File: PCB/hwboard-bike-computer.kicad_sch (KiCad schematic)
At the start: 0 parts

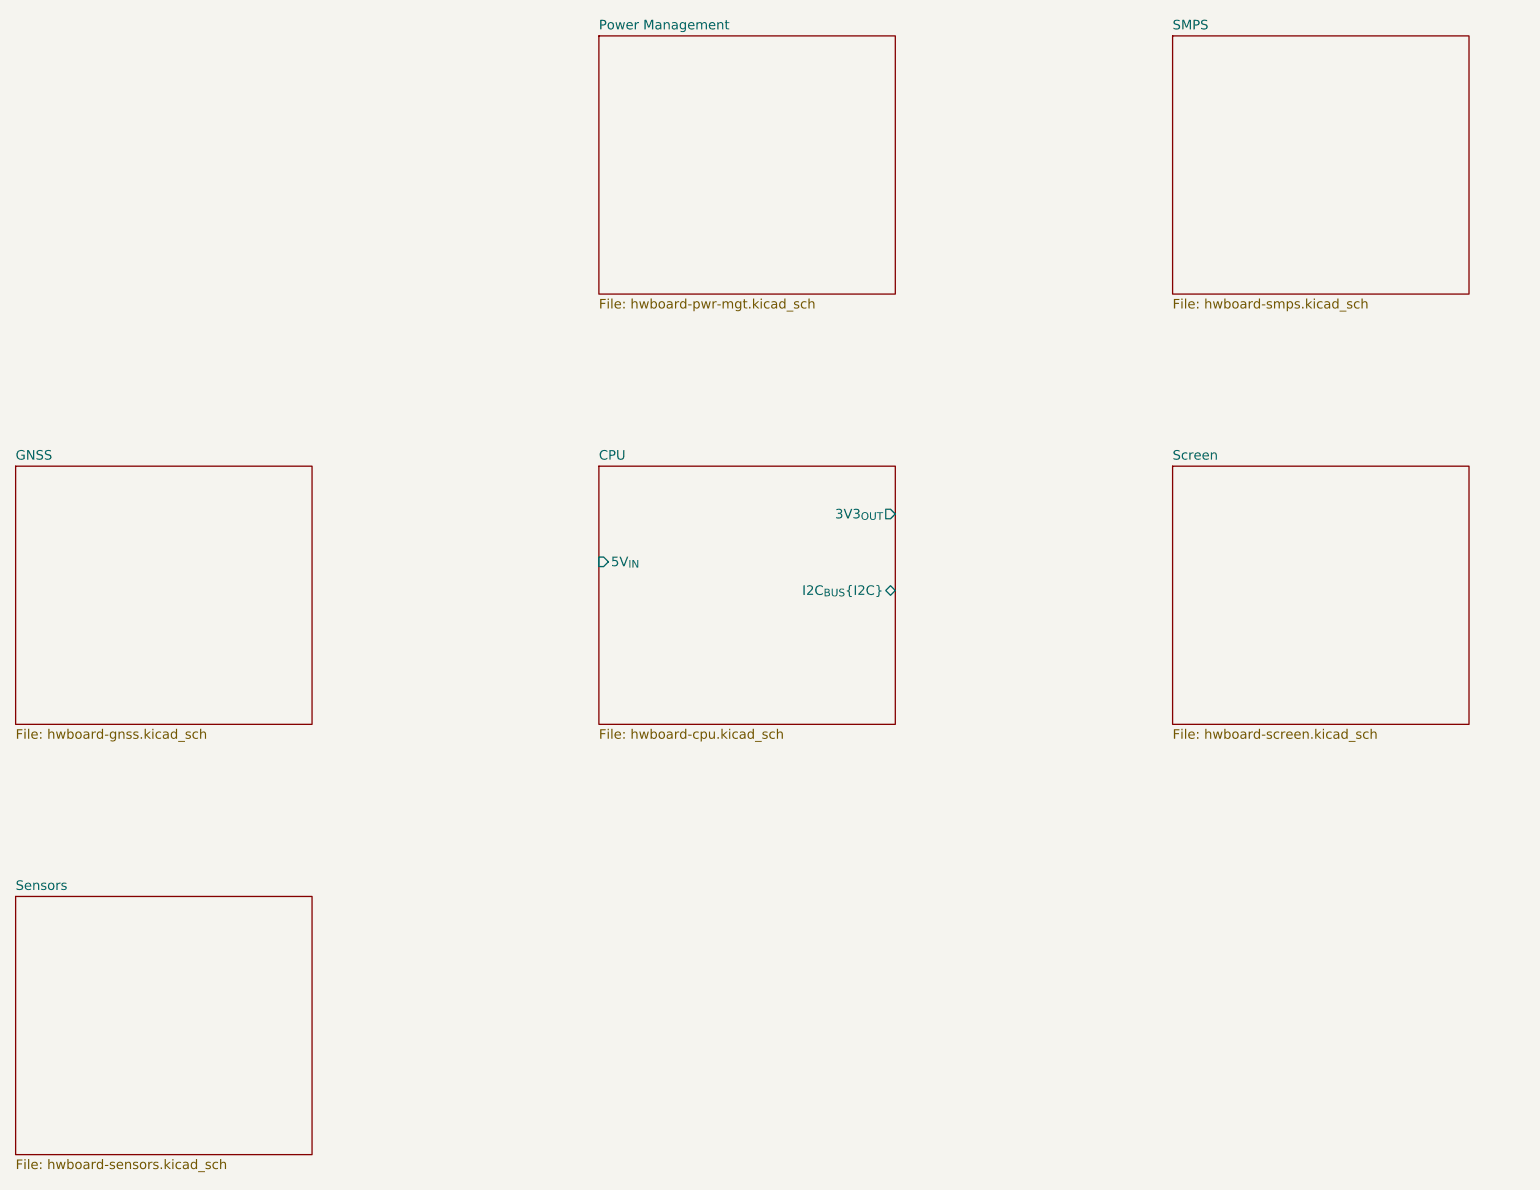
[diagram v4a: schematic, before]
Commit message: add dc dc schematic
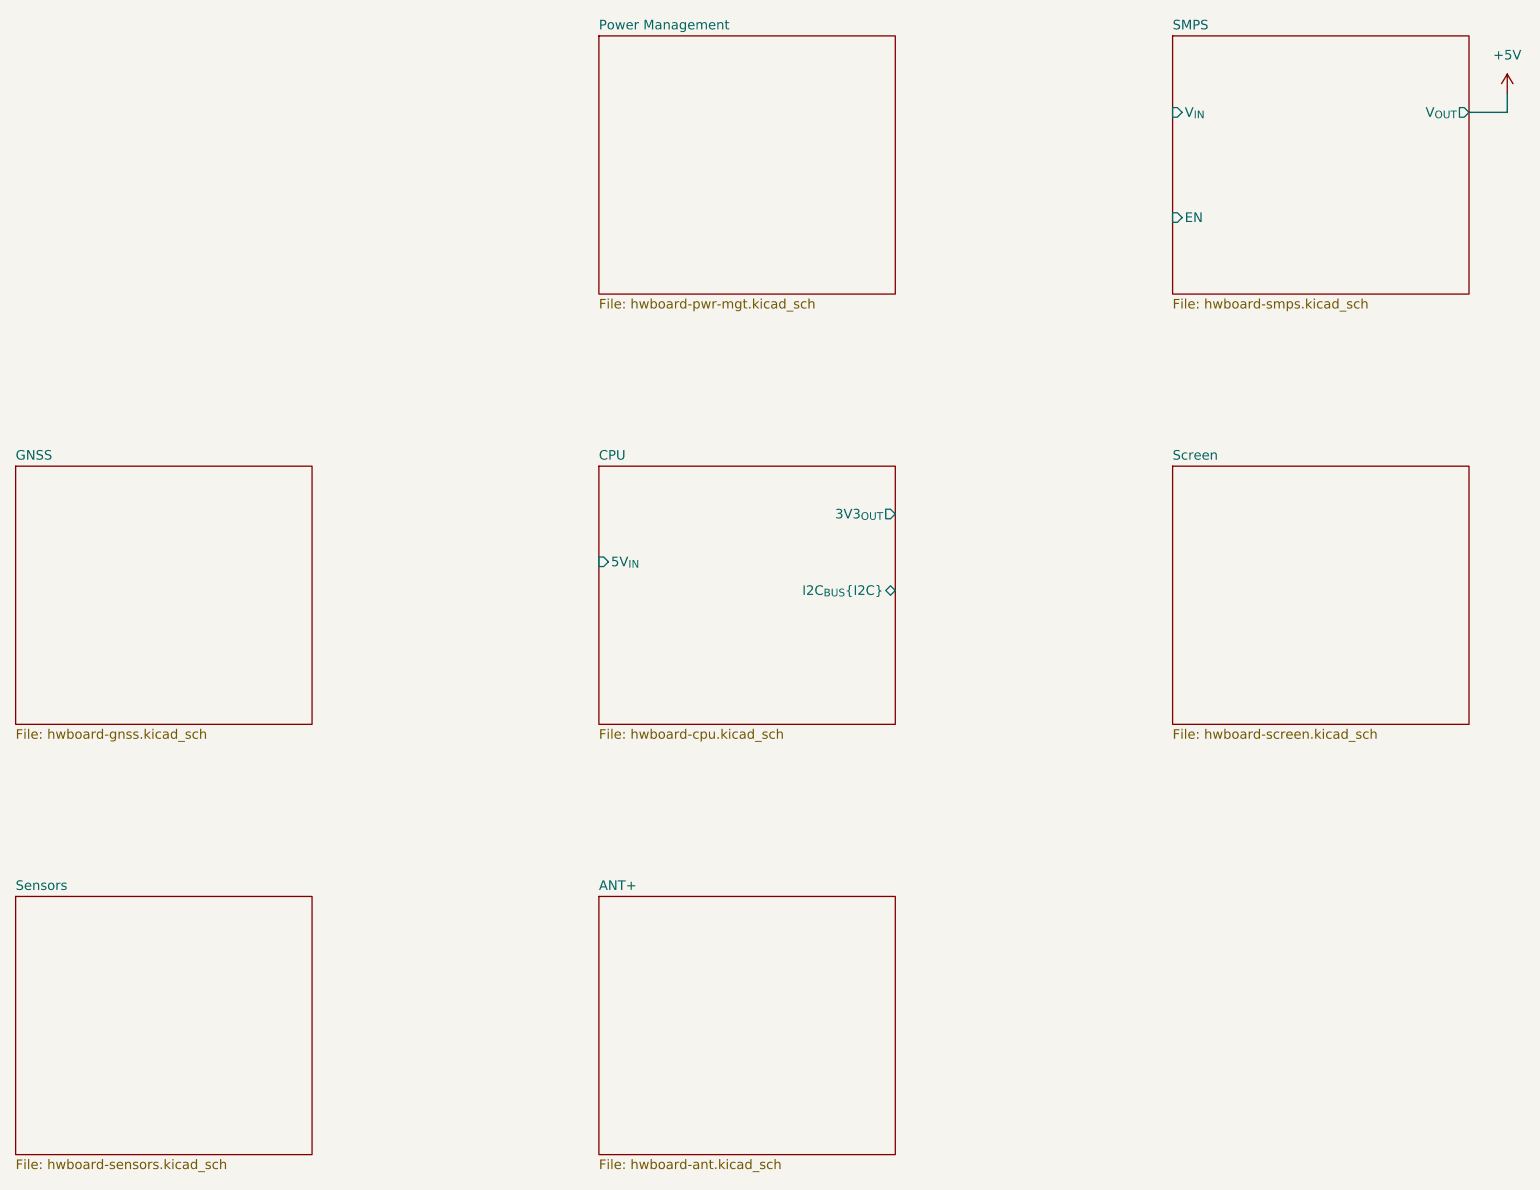
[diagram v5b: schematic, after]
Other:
- added sheet ANT+ (hwboard-ant.kicad_sch)
- sheet SMPS ports: added EN, V_{IN}, V_{OUT}; removed none
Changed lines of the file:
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@@
 		(rev "0.1")
+	)
+	(wire
+		(pts
+			(xy 250.19 35.56) (xy 250.19 38.1)
+		)
+		(stroke
+			(width 0)
+			(type default)
+		)
+	)
+	(wire
+		(pts
+			(xy 250.19 38.1) (xy 245.11 38.1)
+		)
+		(stroke
+			(width 0)
+			(type default)
+		)
+	)
+	(symbol
+		(lib_id "power:+5V")
+		(at 250.19 35.56 0)
+		(unit 1)
+		(exclude_from_sim no)
+		(in_bom yes)
+		(on_board yes)
+		(dnp no)
+		(fields_autoplaced yes)
+		(property "Reference" "#PWR013"
+			(at 250.19 39.37 0)
+			(effects
+				(font
+					(size 1.27 1.27)
+				)
+				(hide yes)
+			)
+		)
+		(property "Value" "+5V"
+			(at 250.19 30.48 0)
+			(effects
+				(font
+					(size 1.27 1.27)
+				)
+			)
+		)
+		(property "Footprint" ""
+			(at 250.19 35.56 0)
+			(effects
+				(font
+					(size 1.27 1.27)
+				)
+				(hide yes)
+			)
+		)
+		(property "Datasheet" ""
+			(at 250.19 35.56 0)
+			(effects
+				(font
+					(size 1.27 1.27)
+				)
+				(hide yes)
+			)
+		)
+		(property "Description" "Power symbol creates a global label with name \"+5V\""
+			(at 250.19 35.56 0)
+			(effects
+				(font
+					(size 1.27 1.27)
+				)
+				(hide yes)
+			)
+		)
+		(pin "1"
+		)
+		(instances
+			(project ""
+				(path "/8c0f76b9-ee42-4bcf-bb95-09772e367402"
+					(reference "#PWR013")
+					(unit 1)
+				)
+			)
+		)
 	)
 	(sheet
@@
 			)
 		)
+		(pin "EN" input
+			(at 205.74 52.07 180)
+			(effects
+				(font
+					(size 1.27 1.27)
+				)
+				(justify left)
+			)
+		)
+		(pin "V_{IN}" input
+			(at 205.74 38.1 180)
+			(effects
+				(font
+					(size 1.27 1.27)
+				)
+				(justify left)
+			)
+		)
+		(pin "V_{OUT}" output
+			(at 245.11 38.1 0)
+			(effects
+				(font
+					(size 1.27 1.27)
+				)
+				(justify right)
+			)
+		)
 		(instances
 			(project "hwboard-bike-computer"
@@
 				)
 			)
+		)
+	)
+	(sheet
+		(at 129.54 142.24)
+		(size 39.37 34.29)
+		(exclude_from_sim no)
+		(in_bom yes)
+		(on_board yes)
+		(dnp no)
+		(fields_autoplaced yes)
+		(stroke
+			(width 0.1524)
+			(type solid)
+		)
+		(fill
+			(color 0 0 0 0.0000)
+		)
+		(property "Sheetname" "ANT+"
+			(at 129.54 141.5284 0)
+			(effects
+				(font
+					(size 1.27 1.27)
+				)
+				(justify left bottom)
+			)
+		)
+		(property "Sheetfile" "hwboard-ant.kicad_sch"
+			(at 129.54 177.1146 0)
+			(effects
+				(font
+					(size 1.27 1.27)
+				)
+				(justify left top)
+			)
+		)
+		(instances
+			(project "hwboard-bike-computer"
+				(path "/8c0f76b9-ee42-4bcf-bb95-09772e367402"
+					(page "8")
+				)
+			)

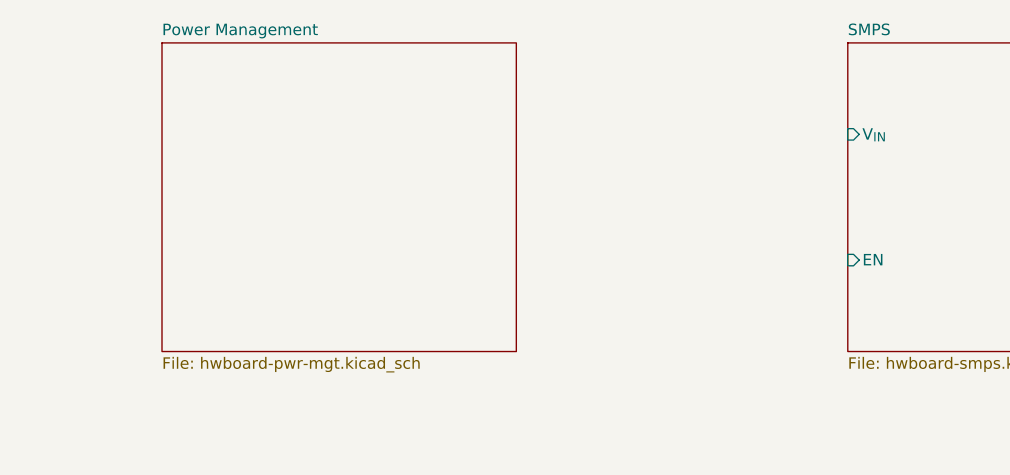
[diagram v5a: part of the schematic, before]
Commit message: add charger and fuel gauge ic
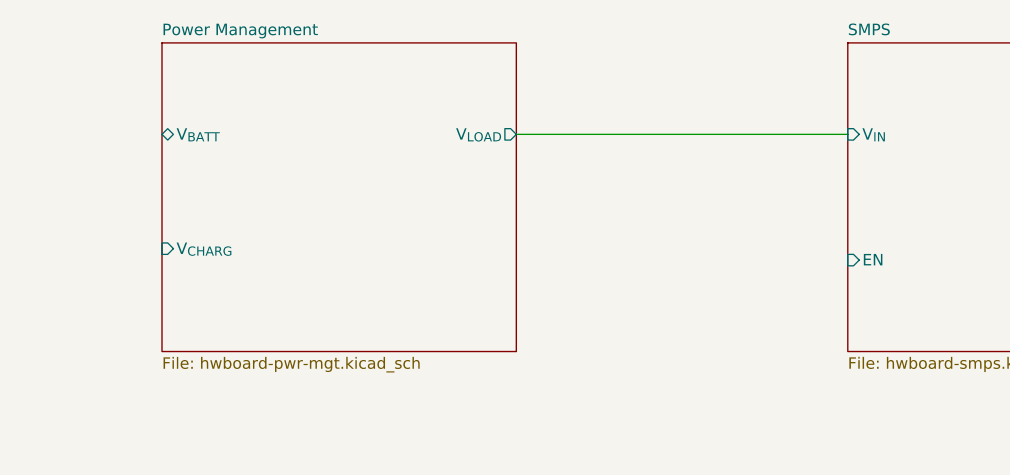
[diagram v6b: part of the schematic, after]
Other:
- sheet Power Management ports: added V_{BATT}, V_{CHARG}, V_{LOAD}; removed none
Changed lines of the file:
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@@
+	(wire
+		(pts
+			(xy 168.91 38.1) (xy 205.74 38.1)
+		)
+		(stroke
+			(width 0)
+			(type default)
+		)
+	)
 	(wire
 		(pts
@@
 			)
 		)
+		(pin "V_{LOAD}" output
+			(at 168.91 38.1 0)
+			(effects
+				(font
+					(size 1.27 1.27)
+				)
+				(justify right)
+			)
+		)
+		(pin "V_{BATT}" bidirectional
+			(at 129.54 38.1 180)
+			(effects
+				(font
+					(size 1.27 1.27)
+				)
+				(justify left)
+			)
+		)
+		(pin "V_{CHARG}" input
+			(at 129.54 50.8 180)
+			(effects
+				(font
+					(size 1.27 1.27)
+				)
+				(justify left)
+			)
+		)

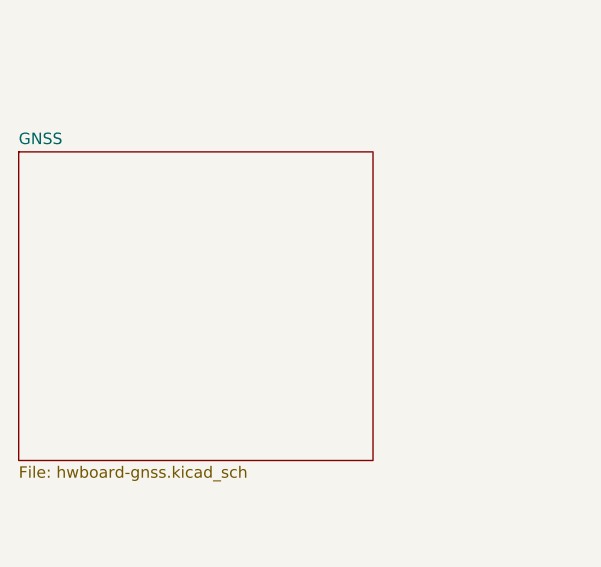
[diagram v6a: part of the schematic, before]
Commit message: Update with gnss
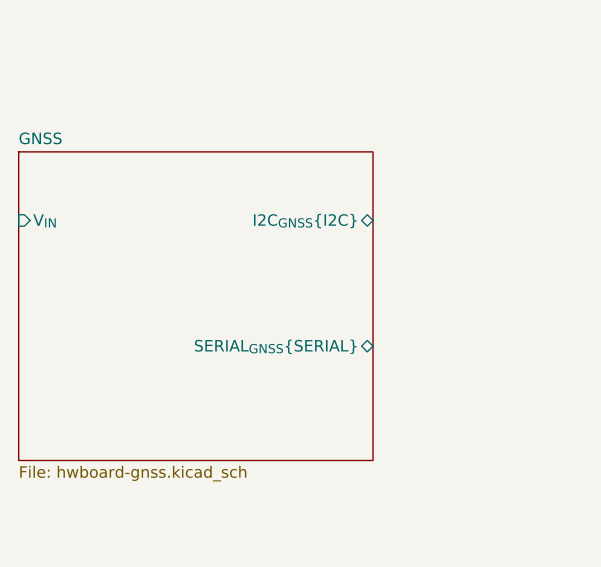
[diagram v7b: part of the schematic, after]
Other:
- sheet GNSS ports: added I2C_{GNSS}{I2C}, SERIAL_{GNSS}{SERIAL}, V_{IN}; removed none
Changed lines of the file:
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@@
 		(rev "0.1")
+	)
+	(bus_alias "SERIAL"
+		(members "TX" "RX")
 	)
 	(wire
@@
 			)
 		)
+		(pin "V_{IN}" input
+			(at 52.07 92.71 180)
+			(effects
+				(font
+					(size 1.27 1.27)
+				)
+				(justify left)
+			)
+		)
+		(pin "I2C_{GNSS}{I2C}" bidirectional
+			(at 91.44 92.71 0)
+			(effects
+				(font
+					(size 1.27 1.27)
+				)
+				(justify right)
+			)
+		)
+		(pin "SERIAL_{GNSS}{SERIAL}" bidirectional
+			(at 91.44 106.68 0)
+			(effects
+				(font
+					(size 1.27 1.27)
+				)
+				(justify right)
+			)
+		)

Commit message: add sensors
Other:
- sheet CPU ports: added SPI_{BUS}{SPI}, UART_{BUS}{SERIAL}; removed none
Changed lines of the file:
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@@
+	(wire
+		(pts
+			(xy 116.84 104.14) (xy 116.84 106.68)
+		)
+		(stroke
+			(width 0)
+			(type default)
+		)
+	)
 	(wire
 		(pts
@@
 		(pts
 			(xy 250.19 38.1) (xy 245.11 38.1)
+		)
+		(stroke
+			(width 0)
+			(type default)
+		)
+	)
+	(wire
+		(pts
+			(xy 123.19 92.71) (xy 123.19 97.79)
+		)
+		(stroke
+			(width 0)
+			(type default)
+		)
+	)
+	(wire
+		(pts
+			(xy 116.84 106.68) (xy 129.54 106.68)
+		)
+		(stroke
+			(width 0)
+			(type default)
+		)
+	)
+	(wire
+		(pts
+			(xy 123.19 97.79) (xy 129.54 97.79)
 		)
 		(stroke
@@
 		)
 	)
+	(symbol
+		(lib_id "power:+3.3V")
+		(at 116.84 104.14 0)
+		(unit 1)
+		(exclude_from_sim no)
+		(in_bom yes)
+		(on_board yes)
+		(dnp no)
+		(fields_autoplaced yes)
+		(property "Reference" "#PWR02"
+			(at 116.84 107.95 0)
+			(effects
+				(font
+					(size 1.27 1.27)
+				)
+				(hide yes)
+			)
+		)
+		(property "Value" "+3.3V"
+			(at 116.84 99.06 0)
+			(effects
+				(font
+					(size 1.27 1.27)
+				)
+			)
+		)
+		(property "Footprint" ""
+			(at 116.84 104.14 0)
+			(effects
+				(font
+					(size 1.27 1.27)
+				)
+				(hide yes)
+			)
+		)
+		(property "Datasheet" ""
+			(at 116.84 104.14 0)
+			(effects
+				(font
+					(size 1.27 1.27)
+				)
+				(hide yes)
+			)
+		)
+		(property "Description" "Power symbol creates a global label with name \"+3.3V\""
+			(at 116.84 104.14 0)
+			(effects
+				(font
+					(size 1.27 1.27)
+				)
+				(hide yes)
+			)
+		)
+		(pin "1"
+		)
+		(instances
+			(project ""
+				(path "/8c0f76b9-ee42-4bcf-bb95-09772e367402"
+					(reference "#PWR02")
+					(unit 1)
+				)
+			)
+		)
+	)
+	(symbol
+		(lib_id "power:+5V")
+		(at 123.19 92.71 0)
+		(unit 1)
+		(exclude_from_sim no)
+		(in_bom yes)
+		(on_board yes)
+		(dnp no)
+		(fields_autoplaced yes)
+		(property "Reference" "#PWR01"
+			(at 123.19 96.52 0)
+			(effects
+				(font
+					(size 1.27 1.27)
+				)
+				(hide yes)
+			)
+		)
+		(property "Value" "+5V"
+			(at 123.19 87.63 0)
+			(effects
+				(font
+					(size 1.27 1.27)
+				)
+			)
+		)
+		(property "Footprint" ""
+			(at 123.19 92.71 0)
+			(effects
+				(font
+					(size 1.27 1.27)
+				)
+				(hide yes)
+			)
+		)
+		(property "Datasheet" ""
+			(at 123.19 92.71 0)
+			(effects
+				(font
+					(size 1.27 1.27)
+				)
+				(hide yes)
+			)
+		)
+		(property "Description" "Power symbol creates a global label with name \"+5V\""
+			(at 123.19 92.71 0)
+			(effects
+				(font
+					(size 1.27 1.27)
+				)
+				(hide yes)
+			)
+		)
+		(pin "1"
+		)
+		(instances
+			(project "hwboard-bike-computer"
+				(path "/8c0f76b9-ee42-4bcf-bb95-09772e367402"
+					(reference "#PWR01")
+					(unit 1)
+				)
+			)
+		)
+	)
 	(sheet
 		(at 52.07 142.24)
@@
 	)
 	(sheet
-		(at 129.54 85.09)
-		(size 39.37 34.29)
+		(at 129.54 86.36)
+		(size 39.37 33.02)
 		(exclude_from_sim no)
 		(in_bom yes)
@@
 		)
 		(property "Sheetname" "CPU"
-			(at 129.54 84.3784 0)
+			(at 129.54 85.6484 0)
 			(effects
 				(font
@@
 		)
 		(pin "3V3_{OUT}" output
+			(at 129.54 106.68 180)
+			(effects
+				(font
+					(size 1.27 1.27)
+				)
+				(justify left)
+			)
+		)
+		(pin "I2C_{BUS}{I2C}" bidirectional
 			(at 168.91 91.44 0)
-			(effects
-				(font
-					(size 1.27 1.27)
-				)
-				(justify right)
-			)
-		)
-		(pin "I2C_{BUS}{I2C}" bidirectional
-			(at 168.91 101.6 0)
 			(effects
 				(font
@@
 			)
 		)
+		(pin "SPI_{BUS}{SPI}" bidirectional
+			(at 168.91 102.87 0)
+			(effects
+				(font
+					(size 1.27 1.27)
+				)
+				(justify right)
+			)
+		)
+		(pin "UART_{BUS}{SERIAL}" bidirectional
+			(at 168.91 114.3 0)
+			(effects
+				(font
+					(size 1.27 1.27)
+				)
+				(justify right)
+			)
+		)
